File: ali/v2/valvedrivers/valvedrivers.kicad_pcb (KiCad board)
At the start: 4 copper layers, 85 x 76 mm, 145 parts, among them J1 Conn_02x01, J10 Conn_01x02, J11 Conn_01x02, J12 Conn_01x02, J13 Conn_01x02, J14 Conn_01x02, J15 Conn_01x02, J16 Conn_01x02, J17 Conn_01x02, J18 Conn_01x02, J19 Conn_01x02, J2 Conn_01x05, J20 Conn_01x02, J21 Conn_01x02, J3 USB_C_Receptacle_USB2.0_16P, J4 Screw_Terminal_01x02, J5 Screw_Terminal_01x02, J6 Screw_Terminal_01x02, J7 Conn_01x05, J8 Vertical Ethernet, J9 Conn_01x03, SW1 SKRPANE010, U1 STM32H563RIV6, U10 SN74CBTLV3245A, U11 IPS4140HQ, U2 LTV-816S, U3 AP2112K-3.3, U4 LTV-816S, U5 LAN8742AI, U6 TJA1462ATK, U7 SN74CBTLV3245A, U8 IPS4140HQ, U9 IPS4140HQ, Y1 25 MHz, Y2 25 MHz

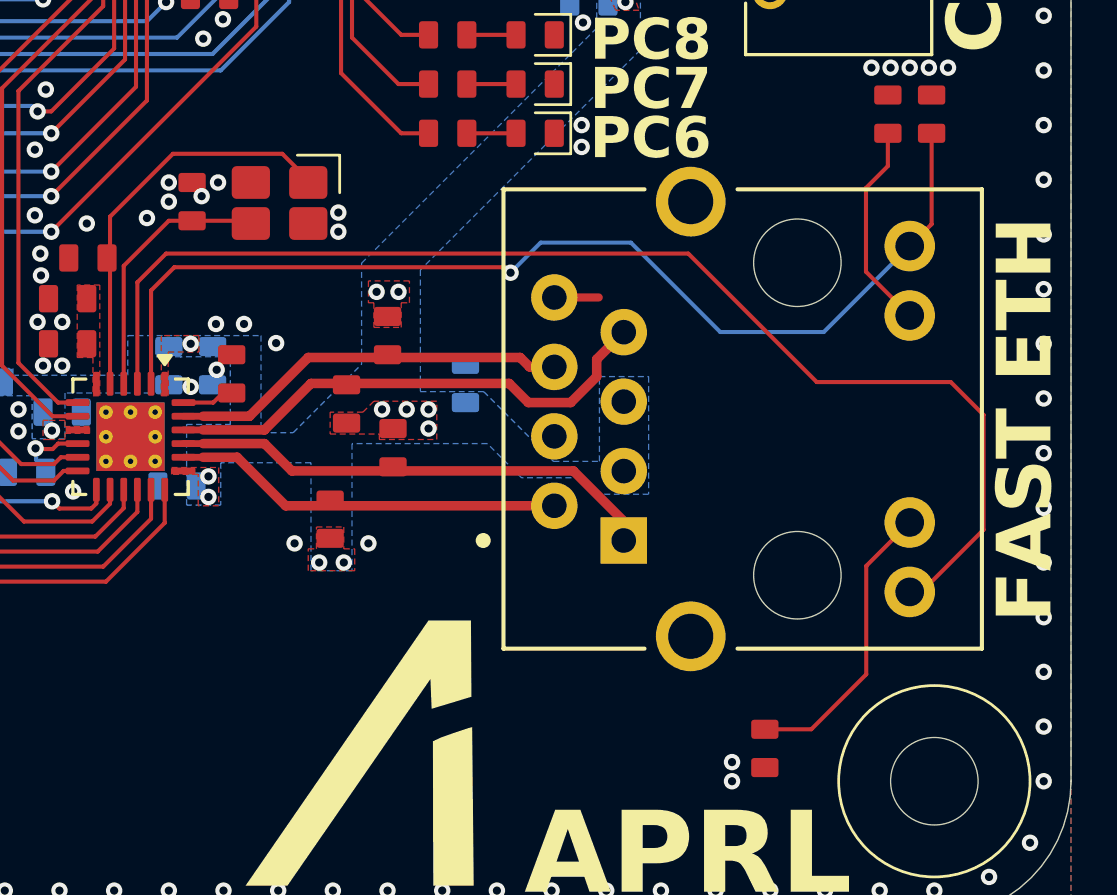
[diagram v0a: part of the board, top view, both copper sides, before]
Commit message: Use 1206 on AFEs
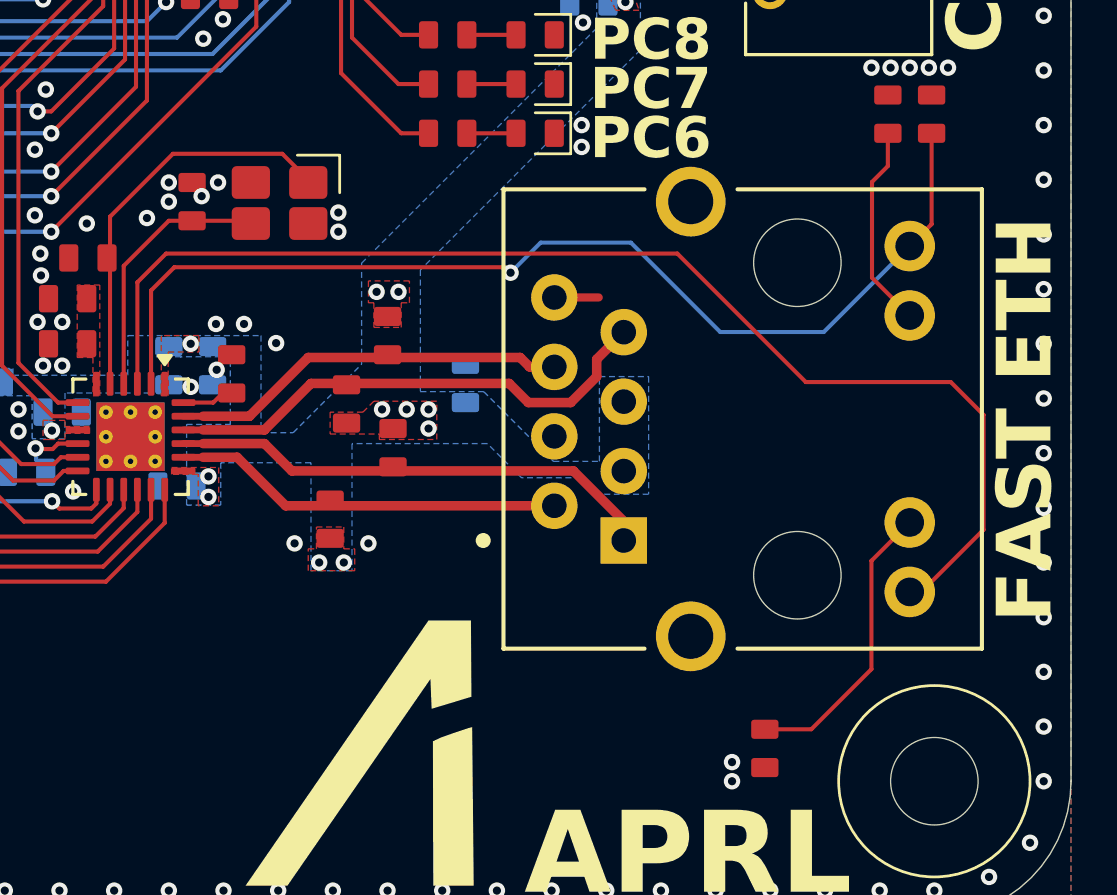
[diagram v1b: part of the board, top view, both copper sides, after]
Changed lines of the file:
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@@
 	)
 	(segment
-		(start 173.2225 126.45)
-		(end 174.8625 124.81)
-		(width 0.15)
-		(layer "F.Cu")
-		(net "Net-(J8-Pad10)")
-	)
-	(segment
-		(start 171.2125 132.425)
-		(end 173.2225 130.415)
+		(start 173.4125 130.225)
+		(end 173.4125 126.26)
 		(width 0.15)
 		(layer "F.Cu")
@@
 	)
 	(segment
-		(start 173.2225 130.415)
-		(end 173.2225 126.45)
+		(start 173.4125 126.26)
+		(end 174.8625 124.81)
+		(width 0.15)
+		(layer "F.Cu")
+		(net "Net-(J8-Pad10)")
+	)
+	(segment
+		(start 171.2125 132.425)
+		(end 173.4125 130.225)
 		(width 0.15)
 		(layer "F.Cu")
@@
 	)
 	(segment
-		(start 173.2125 112.625)
+		(start 173.4325 112.405)
 		(end 174.0125 111.825)
 		(width 0.15)
@@
 	)
 	(segment
+		(start 173.4325 115.91)
+		(end 173.4325 112.405)
+		(width 0.15)
+		(layer "F.Cu")
+		(net "Net-(J8-Pad11)")
+	)
+	(segment
 		(start 174.8125 117.29)
-		(end 173.2125 115.69)
-		(width 0.15)
-		(layer "F.Cu")
-		(net "Net-(J8-Pad11)")
-	)
-	(segment
-		(start 173.2125 115.69)
-		(end 173.2125 112.625)
+		(end 173.4325 115.91)
 		(width 0.15)
 		(layer "F.Cu")
@@
 	)
 	(segment
+		(start 177.5125 120.925)
+		(end 177.5125 125.125)
+		(width 0.15)
+		(layer "F.Cu")
+		(net "Net-(U5-LED1{slash}REGOFF)")
+	)
+	(segment
+		(start 176.3125 119.725)
+		(end 177.5125 120.925)
+		(width 0.15)
+		(layer "F.Cu")
+		(net "Net-(U5-LED1{slash}REGOFF)")
+	)
+	(segment
+		(start 146.5625 119.7875)
+		(end 146.5625 116.075)
+		(width 0.15)
+		(layer "F.Cu")
+		(net "Net-(U5-LED1{slash}REGOFF)")
+	)
+	(segment
+		(start 171.0125 119.725)
+		(end 176.3125 119.725)
+		(width 0.15)
+		(layer "F.Cu")
+		(net "Net-(U5-LED1{slash}REGOFF)")
+	)
+	(segment
 		(start 177.5125 125.125)
 		(end 175.3125 127.325)
@@
 	)
 	(segment
-		(start 176.3125 119.725)
-		(end 177.5125 120.925)
+		(start 147.6125 115.025)
+		(end 166.3125 115.025)
 		(width 0.15)
 		(layer "F.Cu")
@@
 	)
 	(segment
-		(start 166.7125 115.025)
-		(end 171.4125 119.725)
-		(width 0.15)
-		(layer "F.Cu")
-		(net "Net-(U5-LED1{slash}REGOFF)")
-	)
-	(segment
-		(start 177.5125 120.925)
-		(end 177.5125 125.125)
-		(width 0.15)
-		(layer "F.Cu")
-		(net "Net-(U5-LED1{slash}REGOFF)")
-	)
-	(segment
-		(start 147.6125 115.025)
-		(end 166.7125 115.025)
+		(start 166.3125 115.025)
+		(end 171.0125 119.725)
 		(width 0.15)
 		(layer "F.Cu")
@@
 		(width 0.15)
 		(layer "F.Cu")
-		(net "Net-(U5-LED1{slash}REGOFF)")
-	)
-	(segment
-		(start 171.4125 119.725)
-		(end 176.3125 119.725)
-		(width 0.15)
-		(layer "F.Cu")
-		(net "Net-(U5-LED1{slash}REGOFF)")
-	)
-	(segment
-		(start 146.5625 119.7875)
-		(end 146.5625 116.075)
-		(width 0.15)
-		(layer "F.Cu")
